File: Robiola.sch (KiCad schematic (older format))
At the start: 12 parts, among them J1 Conn_01x08, J10 Conn_01x03, J2 Conn_01x08, J3 Conn_01x08, J4 Conn_02x08_Counter_Clockwise, J5 Conn_01x03, J6 Conn_01x03, J7 Conn_01x03, J8 Conn_01x03, J9 Conn_01x03, U1 LM2596, U2 BP

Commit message: adding more component
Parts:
- added BT1: Battery, diy-modules:diy-modules-BATTERY-LI-MH12210, symbol Battery
- added U3: TP4056, diy-modules:diy-modules-BATTERY-CHARGER-LI-5V, symbol TP4056
- J1, J2, J3: footprint (none) -> Pin_Headers:Pin_Header_Straight_1x08_Pitch2.54mm
- J10, J5, J6, J7, J8, J9: footprint (none) -> Pin_Headers:Pin_Header_Straight_1x03_Pitch2.54mm
- J4: footprint (none) -> Pin_Headers:Pin_Header_Straight_2x08_Pitch2.54mm
- U2: footprint (none) -> Housings_DIP:DIP-40_W15.24mm_Socket_LongPads
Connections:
- net at U1.IN+ (Vin): now also BT1.1 (+)
- net at U1.IN- (GND): now also BT1.2 (-)
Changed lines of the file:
@@
 LIBS:contrib
 LIBS:valves
+LIBS:lm2596
+LIBS:tp4056
 LIBS:bluepill
-LIBS:lm2596
 LIBS:Robiola-cache
 EELAYER 26 0
@@
 F 0 "U2" H 3200 3550 60  0000 C CNN
 F 1 "BP" H 3200 3444 60  0000 C CNN
-F 2 "" H 3100 3050 60  0001 C CNN
+F 2 "Housings_DIP:DIP-40_W15.24mm_Socket_LongPads" H 3100 3050 60  0001 C CNN
 F 3 "" H 3100 3050 60  0001 C CNN
 	1    3200 2300
@@
 F 0 "J5" H 6380 1742 50  0000 L CNN
 F 1 "Conn_01x03" H 6380 1651 50  0000 L CNN
-F 2 "" H 6300 1700 50  0001 C CNN
+F 2 "Pin_Headers:Pin_Header_Straight_1x03_Pitch2.54mm" H 6300 1700 50  0001 C CNN
 F 3 "" H 6300 1700 50  0001 C CNN
 	1    6300 1700
@@
 F 0 "J7" H 7280 1742 50  0000 L CNN
 F 1 "Conn_01x03" H 7280 1651 50  0000 L CNN
-F 2 "" H 7200 1700 50  0001 C CNN
+F 2 "Pin_Headers:Pin_Header_Straight_1x03_Pitch2.54mm" H 7200 1700 50  0001 C CNN
 F 3 "" H 7200 1700 50  0001 C CNN
 	1    7200 1700
@@
 F 0 "J9" H 8130 1742 50  0000 L CNN
 F 1 "Conn_01x03" H 8130 1651 50  0000 L CNN
-F 2 "" H 8050 1700 50  0001 C CNN
+F 2 "Pin_Headers:Pin_Header_Straight_1x03_Pitch2.54mm" H 8050 1700 50  0001 C CNN
 F 3 "" H 8050 1700 50  0001 C CNN
 	1    8050 1700
@@
 F 0 "J6" H 6380 2192 50  0000 L CNN
 F 1 "Conn_01x03" H 6380 2101 50  0000 L CNN
-F 2 "" H 6300 2150 50  0001 C CNN
+F 2 "Pin_Headers:Pin_Header_Straight_1x03_Pitch2.54mm" H 6300 2150 50  0001 C CNN
 F 3 "" H 6300 2150 50  0001 C CNN
 	1    6300 2150
@@
 F 0 "J8" H 7280 2192 50  0000 L CNN
 F 1 "Conn_01x03" H 7280 2101 50  0000 L CNN
-F 2 "" H 7200 2150 50  0001 C CNN
+F 2 "Pin_Headers:Pin_Header_Straight_1x03_Pitch2.54mm" H 7200 2150 50  0001 C CNN
 F 3 "" H 7200 2150 50  0001 C CNN
 	1    7200 2150
@@
 F 0 "J10" H 8130 2192 50  0000 L CNN
 F 1 "Conn_01x03" H 8130 2101 50  0000 L CNN
-F 2 "" H 8050 2150 50  0001 C CNN
+F 2 "Pin_Headers:Pin_Header_Straight_1x03_Pitch2.54mm" H 8050 2150 50  0001 C CNN
 F 3 "" H 8050 2150 50  0001 C CNN
 	1    8050 2150
@@
 F 0 "J1" H 1930 2092 50  0000 L CNN
 F 1 "Conn_01x08" H 1930 2001 50  0000 L CNN
-F 2 "" H 1850 2100 50  0001 C CNN
+F 2 "Pin_Headers:Pin_Header_Straight_1x08_Pitch2.54mm" H 1850 2100 50  0001 C CNN
 F 3 "" H 1850 2100 50  0001 C CNN
 	1    1850 2100
@@
 F 0 "J4" H 5750 2317 50  0000 C CNN
 F 1 "Conn_02x08_Counter_Clockwise" H 5750 2226 50  0000 C CNN
-F 2 "" H 5700 1800 50  0001 C CNN
+F 2 "Pin_Headers:Pin_Header_Straight_2x08_Pitch2.54mm" H 5700 1800 50  0001 C CNN
 F 3 "" H 5700 1800 50  0001 C CNN
 	1    5700 1800
@@
 	2050 1900 2450 1900
 Wire Wire Line
-	2050 2000 2450 2000
-Wire Wire Line
 	2050 2100 2450 2100
 Wire Wire Line
@@
 F 0 "J3" H 5169 1275 50  0000 C CNN
 F 1 "Conn_01x08" H 5169 1366 50  0000 C CNN
-F 2 "" H 5250 1900 50  0001 C CNN
+F 2 "Pin_Headers:Pin_Header_Straight_1x08_Pitch2.54mm" H 5250 1900 50  0001 C CNN
 F 3 "" H 5250 1900 50  0001 C CNN
 	1    5250 1900
@@
 F 0 "J2" H 4269 1775 50  0000 C CNN
 F 1 "Conn_01x08" H 4269 1866 50  0000 C CNN
-F 2 "" H 4350 2400 50  0001 C CNN
+F 2 "Pin_Headers:Pin_Header_Straight_1x08_Pitch2.54mm" H 4350 2400 50  0001 C CNN
 F 3 "" H 4350 2400 50  0001 C CNN
 	1    4350 2400
@@
 Text Label 3950 2800 0    60   ~ 0
 PB15
+$Comp
+L Battery BT1
+U 1 1 59CB9739
+P 650 950
+F 0 "BT1" H 758 996 50  0000 L CNN
+F 1 "Battery" H 758 905 50  0000 L CNN
+F 2 "diy-modules:diy-modules-BATTERY-LI-MH12210" V 650 1010 50  0001 C CNN
+F 3 "" V 650 1010 50  0001 C CNN
+	1    650  950
+	1    0    0    -1
+$EndComp
+$Comp
+L TP4056 U3
+U 1 1 59CBA6DD
+P 4500 4050
+F 0 "U3" H 4500 4587 60  0000 C CNN
+F 1 "TP4056" H 4500 4481 60  0000 C CNN
+F 2 "diy-modules:diy-modules-BATTERY-CHARGER-LI-5V" H 4500 4050 60  0001 C CNN
+F 3 "" H 4500 4050 60  0000 C CNN
+	1    4500 4050
+	1    0    0    -1
+$EndComp
+Wire Wire Line
+	2050 2000 2450 2000
+Wire Wire Line
+	650  750  1150 750
+Wire Wire Line
+	1150 1100 1150 1150
+Wire Wire Line
+	1150 1150 650  1150
 $EndSCHEMATC

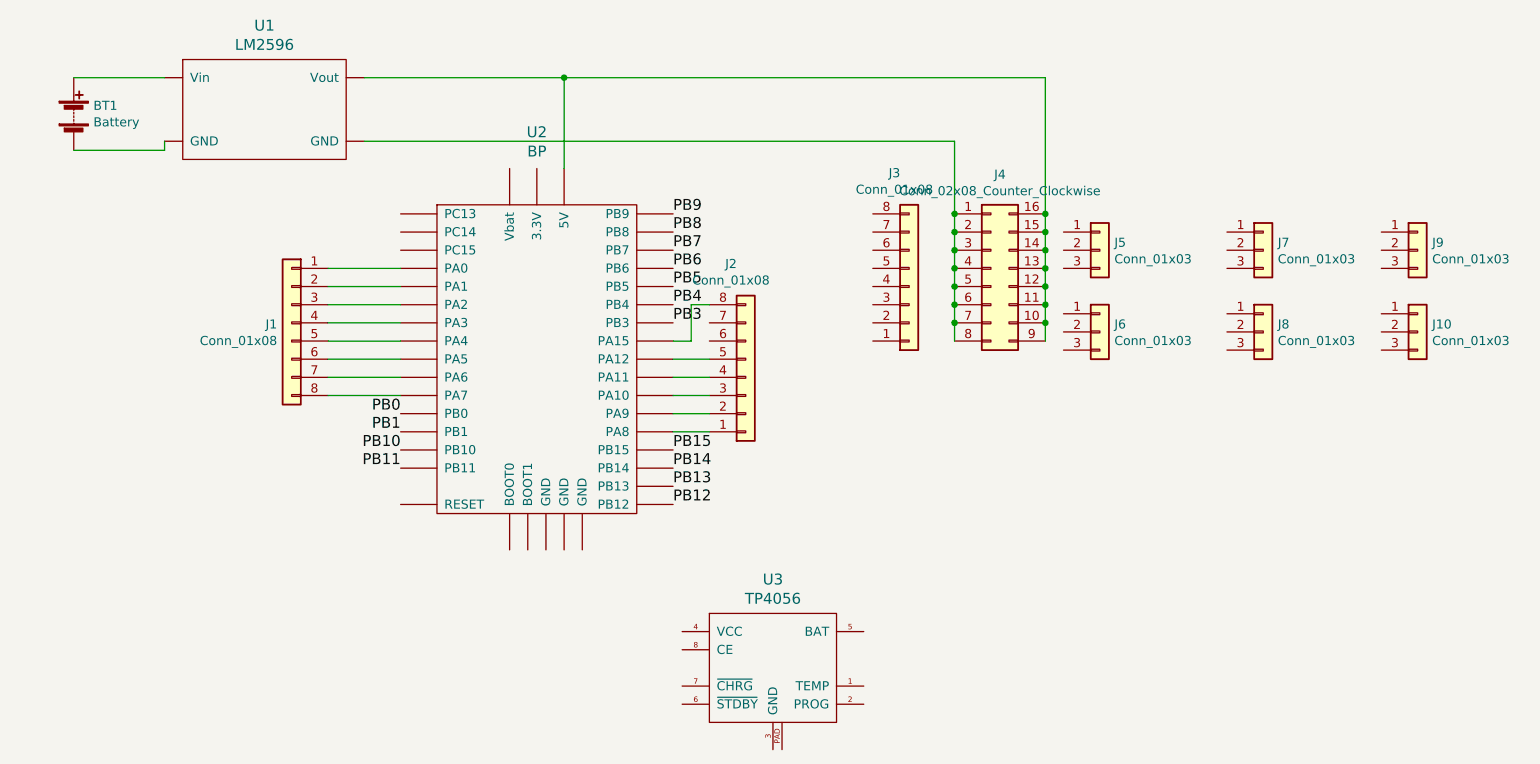
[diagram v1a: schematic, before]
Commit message: add desc in readme, adding some connection
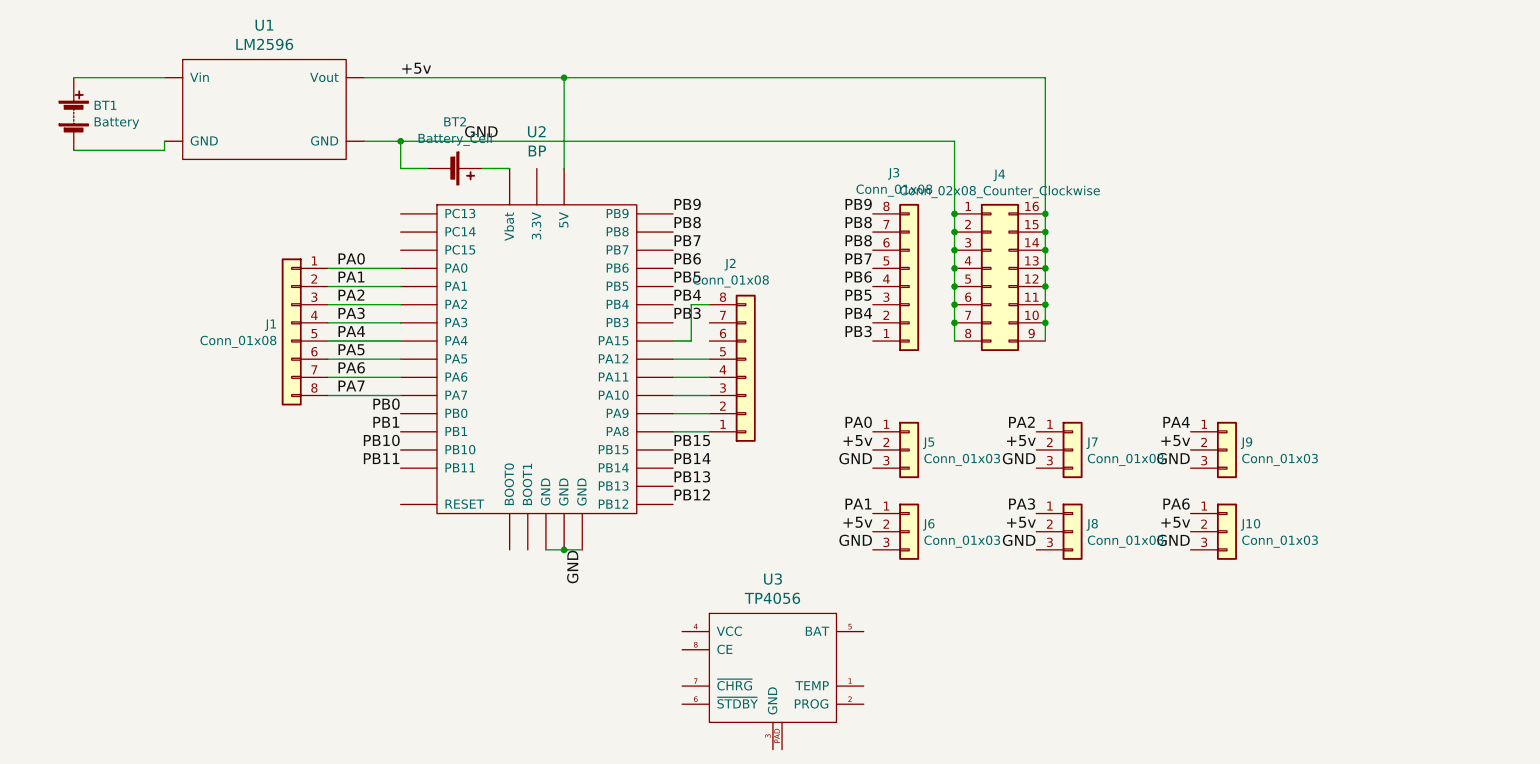
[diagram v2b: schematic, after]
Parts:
- added BT2: Battery_Cell, Battery_Holders:Keystone_104_1x23mm-CoinCell, symbol Battery_Cell
- BT1: footprint diy-modules:diy-modules-BATTERY-LI-MH12210 -> Battery_Holders:Keystone_1042_1x18650
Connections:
- net PB3: now also J3.1 (Pin_1)
- net PB4: now also J3.2 (Pin_2)
- net PB5: now also J3.3 (Pin_3)
- net PB6: now also J3.4 (Pin_4)
- net PB7: now also J3.5 (Pin_5)
- net PB8: now also J3.6 (Pin_6), J3.7 (Pin_7)
- net PB9: now also J3.8 (Pin_8)
- net +5v: now reaches J4.10 (Pin_10), J4.11 (Pin_11), J4.12 (Pin_12), J4.13 (Pin_13), J4.14 (Pin_14), J4.15 (Pin_15), J4.16 (Pin_16), J4.9 (Pin_9), U1.OUT+ (Vout), U2.18 (5V)
- net +5v: now also J10.2 (Pin_2), J5.2 (Pin_2), J6.2 (Pin_2), J7.2 (Pin_2), J8.2 (Pin_2), J9.2 (Pin_2)
- net GND: now reaches U2.19 (GND)
- net GND: now also J10.3 (Pin_3), J4.1 (Pin_1), J4.2 (Pin_2), J4.3 (Pin_3), J4.4 (Pin_4), J4.5 (Pin_5), J4.6 (Pin_6), J4.7 (Pin_7), J4.8 (Pin_8), J5.3 (Pin_3), J6.3 (Pin_3), J7.3 (Pin_3), J8.3 (Pin_3), J9.3 (Pin_3), U1.OUT- (GND), U2.39 (GND), U2.40 (GND), BT2.2 (-)
- net at U2.21 (Vbat): now also BT2.1 (+)
- net PA0: now reaches J1.1 (Pin_1), U2.25 (PA0)
- net PA0: now also J5.1 (Pin_1)
- net PA1: now reaches J1.2 (Pin_2), U2.26 (PA1)
- net PA1: now also J6.1 (Pin_1)
- net PA2: now reaches J1.3 (Pin_3), U2.27 (PA2)
- net PA2: now also J7.1 (Pin_1)
- net PA3: now reaches J1.4 (Pin_4), U2.28 (PA3)
- net PA3: now also J8.1 (Pin_1)
- net PA4: now reaches J1.5 (Pin_5), U2.29 (PA4)
- net PA4: now also J9.1 (Pin_1)
- net PA5: now reaches J1.6 (Pin_6), U2.30 (PA5)
- net PA6: now reaches J1.7 (Pin_7), U2.31 (PA6)
- net PA6: now also J10.1 (Pin_1)
- net PA7: now reaches J1.8 (Pin_8), U2.32 (PA7)
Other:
- moved on the sheet: J10, J5, J6, J7, J8, J9
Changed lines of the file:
@@
 L Conn_01x03 J5
 U 1 1 59BC7E4D
-P 6300 1700
-F 0 "J5" H 6380 1742 50  0000 L CNN
-F 1 "Conn_01x03" H 6380 1651 50  0000 L CNN
-F 2 "Pin_Headers:Pin_Header_Straight_1x03_Pitch2.54mm" H 6300 1700 50  0001 C CNN
-F 3 "" H 6300 1700 50  0001 C CNN
-	1    6300 1700
+P 5250 2800
+F 0 "J5" H 5330 2842 50  0000 L CNN
+F 1 "Conn_01x03" H 5330 2751 50  0000 L CNN
+F 2 "Pin_Headers:Pin_Header_Straight_1x03_Pitch2.54mm" H 5250 2800 50  0001 C CNN
+F 3 "" H 5250 2800 50  0001 C CNN
+	1    5250 2800
 	1    0    0    -1
 $EndComp
@@
 L Conn_01x03 J7
 U 1 1 59BC7ED5
-P 7200 1700
-F 0 "J7" H 7280 1742 50  0000 L CNN
-F 1 "Conn_01x03" H 7280 1651 50  0000 L CNN
-F 2 "Pin_Headers:Pin_Header_Straight_1x03_Pitch2.54mm" H 7200 1700 50  0001 C CNN
-F 3 "" H 7200 1700 50  0001 C CNN
-	1    7200 1700
+P 6150 2800
+F 0 "J7" H 6230 2842 50  0000 L CNN
+F 1 "Conn_01x03" H 6230 2751 50  0000 L CNN
+F 2 "Pin_Headers:Pin_Header_Straight_1x03_Pitch2.54mm" H 6150 2800 50  0001 C CNN
+F 3 "" H 6150 2800 50  0001 C CNN
+	1    6150 2800
 	1    0    0    -1
 $EndComp
@@
 L Conn_01x03 J9
 U 1 1 59BC7F81
-P 8050 1700
-F 0 "J9" H 8130 1742 50  0000 L CNN
-F 1 "Conn_01x03" H 8130 1651 50  0000 L CNN
-F 2 "Pin_Headers:Pin_Header_Straight_1x03_Pitch2.54mm" H 8050 1700 50  0001 C CNN
-F 3 "" H 8050 1700 50  0001 C CNN
-	1    8050 1700
+P 7000 2800
+F 0 "J9" H 7080 2842 50  0000 L CNN
+F 1 "Conn_01x03" H 7080 2751 50  0000 L CNN
+F 2 "Pin_Headers:Pin_Header_Straight_1x03_Pitch2.54mm" H 7000 2800 50  0001 C CNN
+F 3 "" H 7000 2800 50  0001 C CNN
+	1    7000 2800
 	1    0    0    -1
 $EndComp
@@
 L Conn_01x03 J6
 U 1 1 59BC81CC
-P 6300 2150
-F 0 "J6" H 6380 2192 50  0000 L CNN
-F 1 "Conn_01x03" H 6380 2101 50  0000 L CNN
-F 2 "Pin_Headers:Pin_Header_Straight_1x03_Pitch2.54mm" H 6300 2150 50  0001 C CNN
-F 3 "" H 6300 2150 50  0001 C CNN
-	1    6300 2150
+P 5250 3250
+F 0 "J6" H 5330 3292 50  0000 L CNN
+F 1 "Conn_01x03" H 5330 3201 50  0000 L CNN
+F 2 "Pin_Headers:Pin_Header_Straight_1x03_Pitch2.54mm" H 5250 3250 50  0001 C CNN
+F 3 "" H 5250 3250 50  0001 C CNN
+	1    5250 3250
 	1    0    0    -1
 $EndComp
@@
 L Conn_01x03 J8
 U 1 1 59BC81D3
-P 7200 2150
-F 0 "J8" H 7280 2192 50  0000 L CNN
-F 1 "Conn_01x03" H 7280 2101 50  0000 L CNN
-F 2 "Pin_Headers:Pin_Header_Straight_1x03_Pitch2.54mm" H 7200 2150 50  0001 C CNN
-F 3 "" H 7200 2150 50  0001 C CNN
-	1    7200 2150
+P 6150 3250
+F 0 "J8" H 6230 3292 50  0000 L CNN
+F 1 "Conn_01x03" H 6230 3201 50  0000 L CNN
+F 2 "Pin_Headers:Pin_Header_Straight_1x03_Pitch2.54mm" H 6150 3250 50  0001 C CNN
+F 3 "" H 6150 3250 50  0001 C CNN
+	1    6150 3250
 	1    0    0    -1
 $EndComp
@@
 L Conn_01x03 J10
 U 1 1 59BC81DA
-P 8050 2150
-F 0 "J10" H 8130 2192 50  0000 L CNN
-F 1 "Conn_01x03" H 8130 2101 50  0000 L CNN
-F 2 "Pin_Headers:Pin_Header_Straight_1x03_Pitch2.54mm" H 8050 2150 50  0001 C CNN
-F 3 "" H 8050 2150 50  0001 C CNN
-	1    8050 2150
+P 7000 3250
+F 0 "J10" H 7080 3292 50  0000 L CNN
+F 1 "Conn_01x03" H 7080 3201 50  0000 L CNN
+F 2 "Pin_Headers:Pin_Header_Straight_1x03_Pitch2.54mm" H 7000 3250 50  0001 C CNN
+F 3 "" H 7000 3250 50  0001 C CNN
+	1    7000 3250
 	1    0    0    -1
 $EndComp
@@
 F 0 "BT1" H 758 996 50  0000 L CNN
 F 1 "Battery" H 758 905 50  0000 L CNN
-F 2 "diy-modules:diy-modules-BATTERY-LI-MH12210" V 650 1010 50  0001 C CNN
+F 2 "Battery_Holders:Keystone_1042_1x18650" V 650 1010 50  0001 C CNN
 F 3 "" V 650 1010 50  0001 C CNN
 	1    650  950
@@
 Wire Wire Line
 	1150 1150 650  1150
+Text Label 2450 750  0    60   ~ 0
++5v
+Text Label 6800 3250 2    60   ~ 0
++5v
+Text Label 6800 2800 2    60   ~ 0
++5v
+Text Label 5950 3250 2    60   ~ 0
++5v
+Text Label 5950 2800 2    60   ~ 0
++5v
+Text Label 5050 2800 2    60   ~ 0
++5v
+Text Label 5050 3250 2    60   ~ 0
++5v
+Text Label 2800 1100 0    60   ~ 0
+GND
+Text Label 5050 2900 2    60   ~ 0
+GND
+Text Label 5950 2900 2    60   ~ 0
+GND
+Text Label 6800 2900 2    60   ~ 0
+GND
+Text Label 6800 3350 2    60   ~ 0
+GND
+Text Label 5950 3350 2    60   ~ 0
+GND
+Text Label 5050 3350 2    60   ~ 0
+GND
+Wire Wire Line
+	3250 3350 3450 3350
+Connection ~ 3350 3350
+Text Label 3450 3350 3    60   ~ 0
+GND
+$Comp
+L Battery_Cell BT2
+U 1 1 59CC5E06
+P 2700 1250
+F 0 "BT2" V 2445 1300 50  0000 C CNN
+F 1 "Battery_Cell" V 2536 1300 50  0000 C CNN
+F 2 "Battery_Holders:Keystone_104_1x23mm-CoinCell" V 2700 1310 50  0001 C CNN
+F 3 "" V 2700 1310 50  0001 C CNN
+	1    2700 1250
+	0    1    1    0
+$EndComp
+Wire Wire Line
+	2900 1250 3050 1250
+Wire Wire Line
+	2600 1250 2450 1250
+Wire Wire Line
+	2450 1250 2450 1100
+Connection ~ 2450 1100
+Text Label 2100 1800 0    60   ~ 0
+PA0
+Text Label 2100 1900 0    60   ~ 0
+PA1
+Text Label 2100 2000 0    60   ~ 0
+PA2
+Text Label 2100 2100 0    60   ~ 0
+PA3
+Text Label 2100 2200 0    60   ~ 0
+PA4
+Text Label 2100 2300 0    60   ~ 0
+PA5
+Text Label 2100 2400 0    60   ~ 0
+PA6
+Text Label 2100 2500 0    60   ~ 0
+PA7
+Text Label 5050 2700 2    60   ~ 0
+PA0
+Text Label 5050 3150 2    60   ~ 0
+PA1
+Text Label 5950 2700 2    60   ~ 0
+PA2
+Text Label 5950 3150 2    60   ~ 0
+PA3
+Text Label 6800 2700 2    60   ~ 0
+PA4
+Text Label 6800 3150 2    60   ~ 0
+PA6
+Text Label 5050 2200 2    60   ~ 0
+PB3
+Text Label 5050 2100 2    60   ~ 0
+PB4
+Text Label 5050 2000 2    60   ~ 0
+PB5
+Text Label 5050 1900 2    60   ~ 0
+PB6
+Text Label 5050 1800 2    60   ~ 0
+PB7
+Text Label 5050 1700 2    60   ~ 0
+PB8
+Text Label 5050 1600 2    60   ~ 0
+PB8
+Text Label 5050 1500 2    60   ~ 0
+PB9
 $EndSCHEMATC

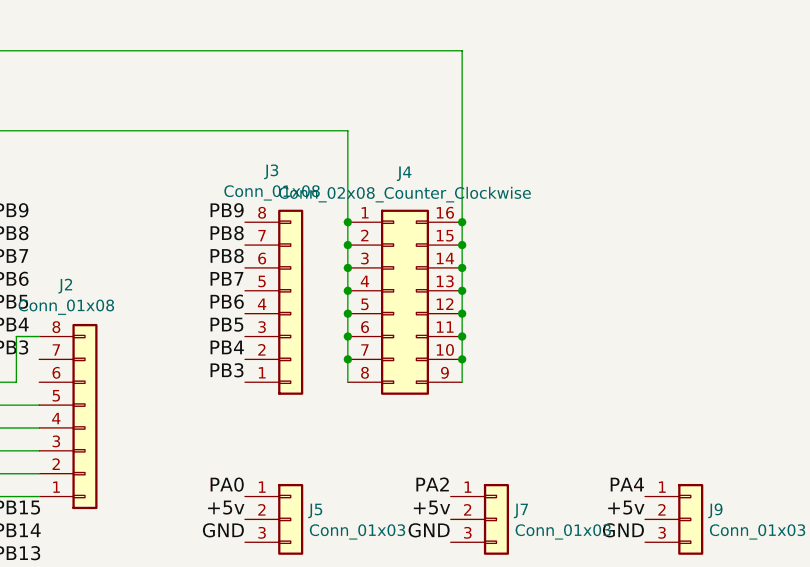
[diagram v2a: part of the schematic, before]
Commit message: fixing a header, adding size estimation, add wanted feature to README
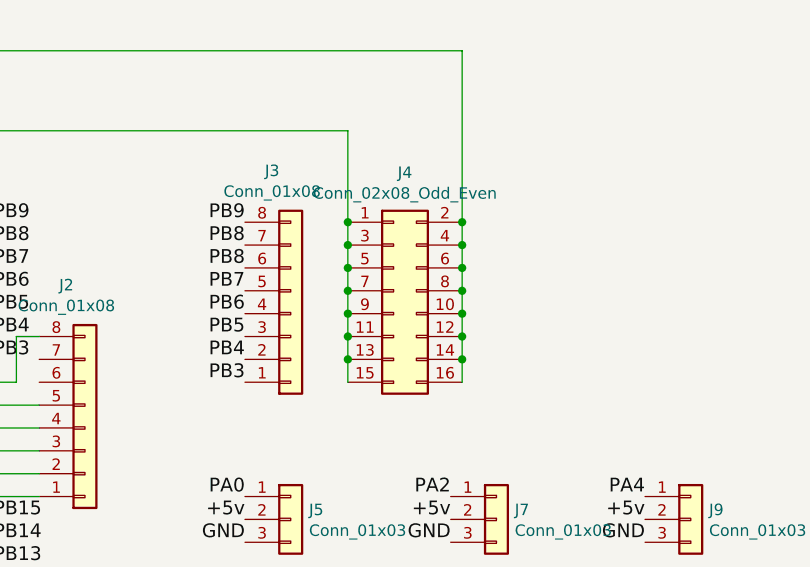
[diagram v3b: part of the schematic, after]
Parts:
- removed J4: Conn_02x08_Counter_Clockwise, Pin_Headers:Pin_Header_Straight_2x08_Pitch2.54mm, symbol Conn_02x08_Counter_Clockwise
- added J4: Conn_02x08_Odd_Even, symbol Conn_02x08_Odd_Even
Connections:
- net +5v: now also J4.10 (Pin_10), J4.12 (Pin_12), J4.14 (Pin_14), J4.16 (Pin_16), J4.2 (Pin_2), J4.4 (Pin_4), J4.6 (Pin_6), J4.8 (Pin_8)
- net GND: now also J4.1 (Pin_1), J4.11 (Pin_11), J4.13 (Pin_13), J4.15 (Pin_15), J4.3 (Pin_3), J4.5 (Pin_5), J4.7 (Pin_7), J4.9 (Pin_9)
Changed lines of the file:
@@
-EESchema Schematic File Version 2
+EESchema Schematic File Version 3
 LIBS:power
 LIBS:device
@@
 $EndComp
 $Comp
-L Conn_02x08_Counter_Clockwise J4
-U 1 1 59BC840E
-P 5700 1800
-F 0 "J4" H 5750 2317 50  0000 C CNN
-F 1 "Conn_02x08_Counter_Clockwise" H 5750 2226 50  0000 C CNN
-F 2 "Pin_Headers:Pin_Header_Straight_2x08_Pitch2.54mm" H 5700 1800 50  0001 C CNN
-F 3 "" H 5700 1800 50  0001 C CNN
-	1    5700 1800
-	1    0    0    -1
-$EndComp
-$Comp
 L LM2596 U1
 U 1 1 59BC8681
@@
 Text Label 5050 1500 2    60   ~ 0
 PB9
+$Comp
+L Conn_02x08_Odd_Even J4
+U 1 1 59CD101B
+P 5700 1800
+F 0 "J4" H 5750 2317 50  0000 C CNN
+F 1 "Conn_02x08_Odd_Even" H 5750 2226 50  0000 C CNN
+F 2 "" H 5700 1800 50  0001 C CNN
+F 3 "" H 5700 1800 50  0001 C CNN
+	1    5700 1800
+	1    0    0    -1
+$EndComp
 $EndSCHEMATC

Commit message: finishing ver 1
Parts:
- removed BT1: Battery, Battery_Holders:Keystone_1042_1x18650, symbol Battery
- removed BT2: Battery_Cell, Battery_Holders:Keystone_104_1x23mm-CoinCell, symbol Battery_Cell
- removed J10, J5, J6, J7, J8, J9: Conn_01x03, Pin_Headers:Pin_Header_Straight_1x03_Pitch2.54mm, symbol Conn_01x03
- removed J2: Conn_01x08, Pin_Headers:Pin_Header_Straight_1x08_Pitch2.54mm, symbol Conn_01x08
- removed U3: TP4056, diy-modules:diy-modules-BATTERY-CHARGER-LI-5V, symbol TP4056
- added D1: LED, LEDs:LED_D3.0mm, symbol device:LED
- added J11, J12: Conn_02x02_Odd_Even, Pin_Headers:Pin_Header_Straight_2x02_Pitch2.54mm, symbol Connector:Conn_02x02_Odd_Even
- added J2: Conn_01x06, Pin_Headers:Pin_Header_Straight_1x06_Pitch2.54mm, symbol Connector:Conn_01x06
- added J5: Conn_02x08_Odd_Even, Pin_Headers:Pin_Header_Straight_2x08_Pitch2.54mm, symbol Robiola-rescue:Conn_02x08_Odd_Even-RESCUE-Robiola
- added J6: Conn_01x08, Pin_Headers:Pin_Header_Straight_1x08_Pitch2.54mm, symbol Robiola-rescue:Conn_01x08-RESCUE-Robiola
- added J7: Conn_01x03, Pin_Headers:Pin_Header_Straight_1x03_Pitch2.54mm, symbol Connector:Conn_01x03
- added J8: Barrel_Jack, Connectors:BARREL_JACK, symbol Connector:Barrel_Jack
- added R1: 330, Resistors_THT:R_Axial_DIN0204_L3.6mm_D1.6mm_P5.08mm_Horizontal, symbol device:R
- added SW1: SW_DPDT_x2, Buttons_Switches_THT:SW_CuK_JS202011CQN_DPDT_Straight, symbol Switch:SW_DPDT_x2
- J1, J3: symbol Conn_01x08 -> Robiola-rescue:Conn_01x08-RESCUE-Robiola
- J4: footprint (none) -> Pin_Headers:Pin_Header_Straight_2x08_Pitch2.54mm; symbol Conn_02x08_Odd_Even -> Robiola-rescue:Conn_02x08_Odd_Even-RESCUE-Robiola
- U1: symbol LM2596 -> lm2596:LM2596
- U2: symbol BP -> bluepill:BP
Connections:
- net GND: now also J12.1 (Pin_1), J12.3 (Pin_3), J5.1 (Pin_1), J5.11 (Pin_11), J5.13 (Pin_13), J5.15 (Pin_15), J5.3 (Pin_3), J5.5 (Pin_5), J5.7 (Pin_7), J5.9 (Pin_9), J7.3 (Pin_3), R1.1
- net PA0: now also J6.1 (Pin_1)
- net PA1: now also J6.2 (Pin_2)
- net PA2: now also J6.3 (Pin_3)
- net PA3: now also J6.4 (Pin_4)
- net PA4: now also J6.5 (Pin_5)
- net PA5: now also J6.6 (Pin_6)
- net PA6: now also J6.7 (Pin_7)
- net PA7: now also J6.8 (Pin_8)
- net PB10: now also J7.1 (Pin_1)
- net PB11: now also J7.2 (Pin_2)
- net PB8: no longer J3.7 (Pin_7)
- net PB9: now also J3.7 (Pin_7); no longer J3.8 (Pin_8)
- net at U2.10 (PA15): now also J2.6 (Pin_6)
- net at U2.21 (Vbat): now also J12.2 (Pin_2), J12.4 (Pin_4)
- net at U2.5 (PA8): now also J2.1 (Pin_1)
- net at U2.6 (PA9): now also J2.2 (Pin_2)
- net at U2.7 (PA10): now also J2.3 (Pin_3)
- net at U2.8 (PA11): now also J2.4 (Pin_4)
- net at U2.9 (PA12): now also J2.5 (Pin_5)
- net at U1.IN+ (Vin): now also SW1.1 (A)
- net at U1.IN- (GND): now also J11.3 (Pin_3), J11.4 (Pin_4), J8.2
- net +5v renamed +5V
- net +5V: now also J3.8 (Pin_8), D1.2 (A), J5.10 (Pin_10), J5.12 (Pin_12), J5.14 (Pin_14), J5.16 (Pin_16), J5.2 (Pin_2), J5.4 (Pin_4), J5.6 (Pin_6), J5.8 (Pin_8)
- new net: J11.1 (Pin_1), J11.2 (Pin_2), J8.1, SW1.2 (B)
- new net: D1.1 (K), R1.2
